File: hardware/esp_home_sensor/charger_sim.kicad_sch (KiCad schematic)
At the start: 13 parts, among them U1 BQ25170

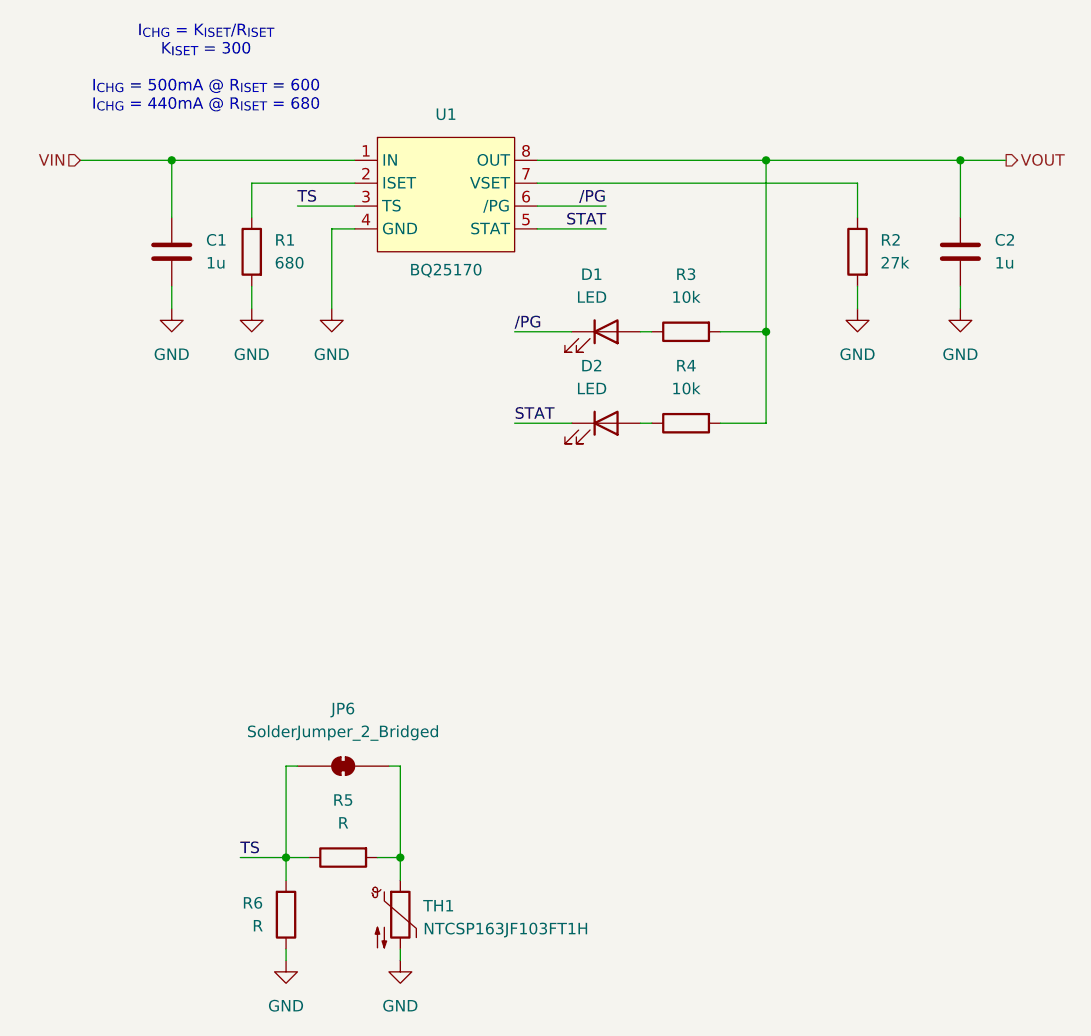
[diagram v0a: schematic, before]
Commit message: footprint assignment, buck
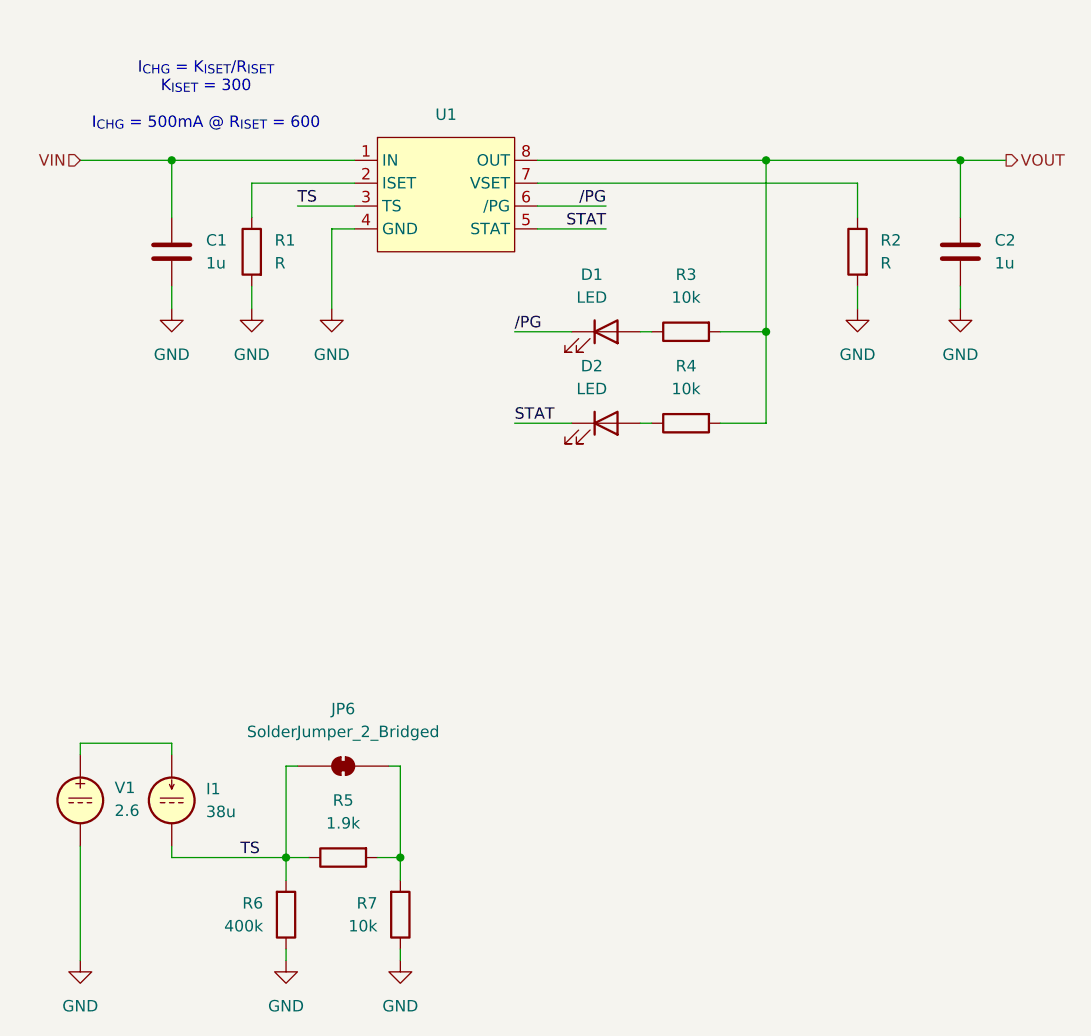
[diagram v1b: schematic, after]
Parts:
- removed TH1: NTCSP163JF103FT1H, Resistor_SMD:R_0603_1608Metric, symbol Device:Thermistor_NTC
- added I1: 38u, symbol Simulation_SPICE:IDC
- added R7: 10k, symbol Device:R
- added V1: 2.6, symbol Simulation_SPICE:VDC
- C1, C2: footprint Capacitor_SMD:C_0402_1005Metric -> (none)
- D1, D2: footprint LED_SMD:LED_0402_1005Metric -> (none)
- R1: value 680 -> R; footprint Resistor_SMD:R_0402_1005Metric -> (none)
- R2: value 27k -> R; footprint Resistor_SMD:R_0402_1005Metric -> (none)
- R3, R4: footprint Resistor_SMD:R_0402_1005Metric -> (none)
- R5: value R -> 1.9k; footprint Resistor_SMD:R_0402_1005Metric -> (none); now in the parts list
- R6: value R -> 400k; footprint Resistor_SMD:R_0402_1005Metric -> (none); now in the parts list
- U1: value BQ25170 -> (none); footprint esp_home_sensor:QFN-8_EP_2x2_Pitch0.5mm -> (none); Mfr. No. BQ25170JDSGR -> (none)
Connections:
- net GND: now also R7.1, V1.2
- net TS: now also I1.2
- net at JP6.2 (B), R5.2: now also R7.2
- new net: I1.1, V1.1
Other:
- note added: "I_{CHG} = K_{ISET}/R_{ISET} K_{ISET} = 300 I_{CHG} = 500mA @ R_{ISET} = 600"
- note removed: "I_{CHG} = K_{ISET}/R_{ISET} K_{ISET} = 300 I_{CHG} = 500mA @ R_{ISET} = 600 I_{CHG} = 440mA @ R_{ISET} = 680"
